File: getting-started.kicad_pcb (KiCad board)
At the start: 2 copper layers, 45 x 36 mm, 3 parts

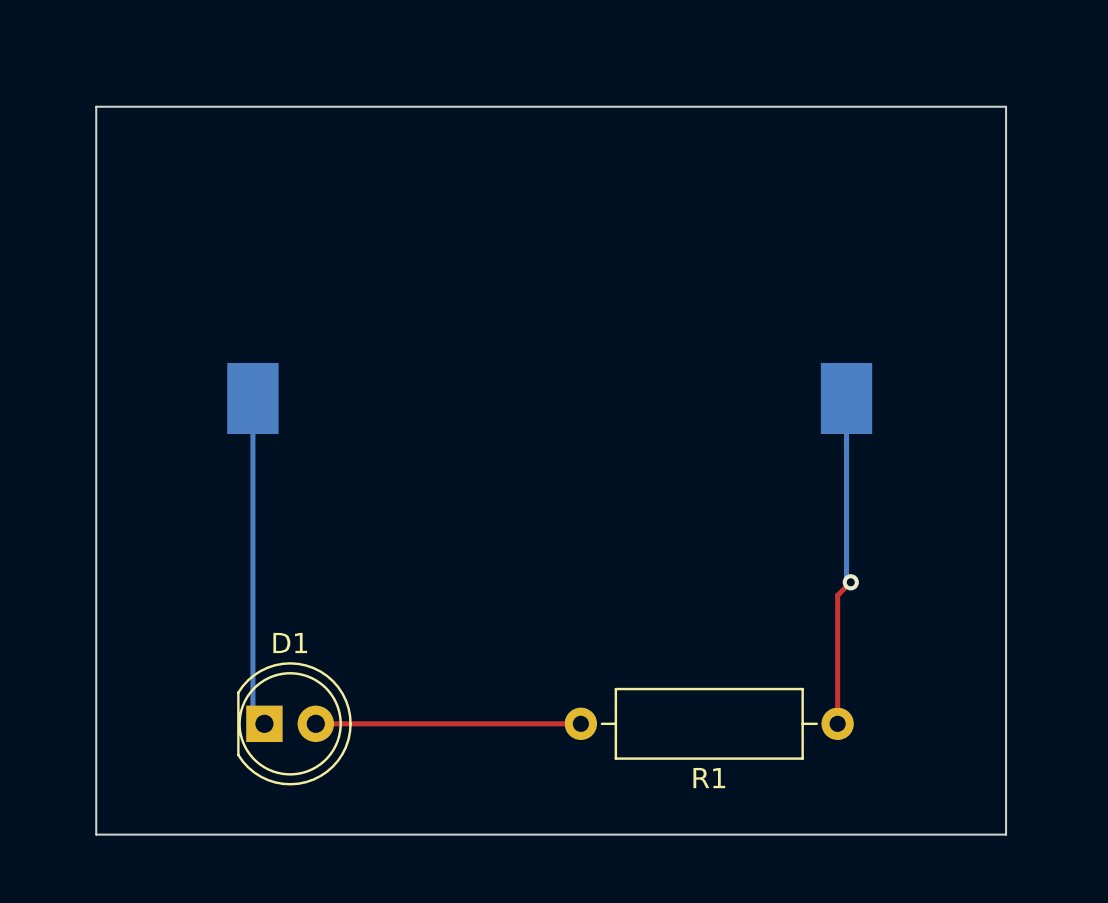
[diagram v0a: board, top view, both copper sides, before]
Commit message: Copper Zones have been added
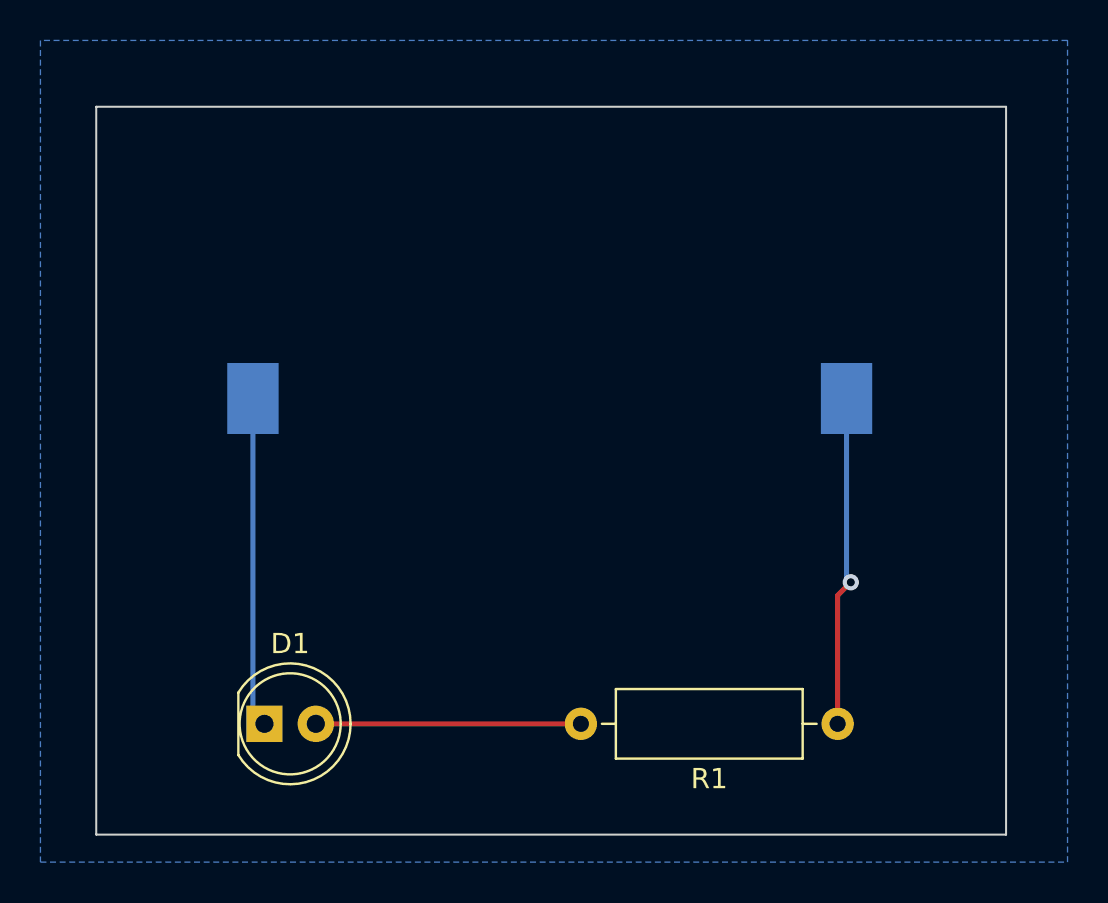
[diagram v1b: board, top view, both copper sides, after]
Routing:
- added copper zone on B.Cu, net GND
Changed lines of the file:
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@@
   (segment (start 132.43 109.43) (end 133 110) (width 0.25) (layer "B.Cu") (net 2))
   (segment (start 135.54 110) (end 148.65 110) (width 0.25) (layer "F.Cu") (net 3))
+  (zone (net 2) (net_name "GND") (layer "B.Cu") (hatch edge 0.5)
+    (connect_pads (clearance 0.5))
+    (min_thickness 0.25) (filled_areas_thickness no)
+    (fill yes (thermal_gap 0.5) (thermal_bridge_width 0.5))
+    (polygon
+      (pts
+        (xy 121.92 76.2)
+        (xy 121.92 116.84)
+        (xy 172.72 116.84)
+        (xy 172.72 76.2)
+      )
+    )
+  )
 )
